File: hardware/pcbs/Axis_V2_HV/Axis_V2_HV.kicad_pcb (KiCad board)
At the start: 2 copper layers, 86.4 x 66 mm, 28 parts, among them J1 SWD, J2 UART, J3 Conn_01x02, J4 Conn_01x02, J5 Conn_01x04, J6 Conn_01x10, J7 Conn_01x08, SW1 RES, U1 Pico, U2 MAX31855EASA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

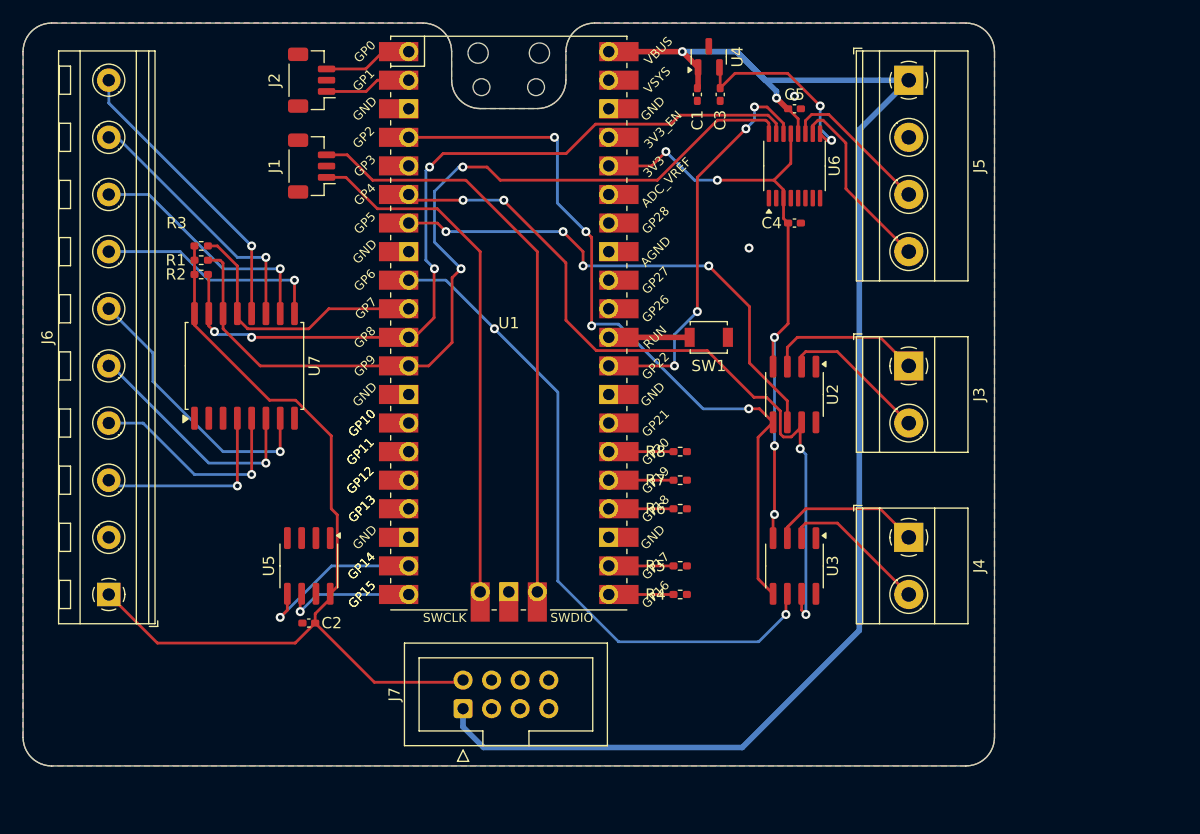
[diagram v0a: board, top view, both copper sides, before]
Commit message: Updates to V2 pcb, add HV pcb
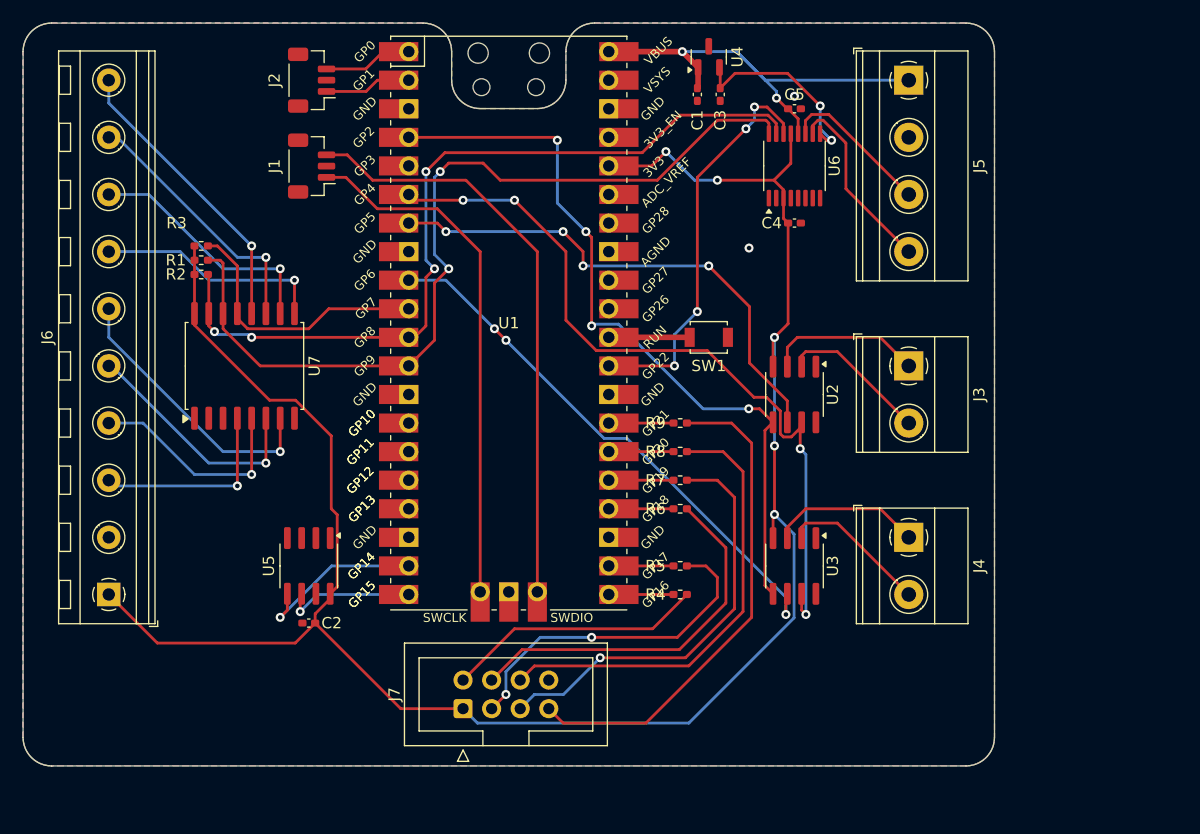
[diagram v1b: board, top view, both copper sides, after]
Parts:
- added R9: 1k, Resistor_SMD:R_0402_1005Metric_Pad0.72x0.64mm_HandSolder, F.Cu at (115.9, 55.6)
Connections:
- J7 pad 1: +5V -> +3V3
- J7 pad 2: +3V3 -> Net-(J7-Pin_2)
- R4 pad 1: Net-(J7-Pin_3) -> Net-(J7-Pin_2)
- R5 pad 1: Net-(J7-Pin_4) -> Net-(J7-Pin_3)
- R6 pad 1: Net-(J7-Pin_5) -> Net-(J7-Pin_4)
- R7 pad 1: Net-(J7-Pin_6) -> Net-(J7-Pin_5)
- R8 pad 1: Net-(J7-Pin_7) -> Net-(J7-Pin_6)
- U1 pad 27: unconnected-(U1-GPIO21-Pad27) -> /HV_IO6
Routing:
- net +5V: track 133.8 -> 41.2 mm
- net +3V3: track 133.8 -> 178.4 mm
- net Net-(J7-Pin_7): track 0.00 -> 44.4 mm
- net Net-(J7-Pin_6): track 0.00 -> 40.5 mm
- net Net-(J7-Pin_5): track 0.00 -> 37.5 mm, vias 0 -> 1
- net Net-(J7-Pin_4): track 0.00 -> 33.5 mm
- net Net-(J7-Pin_3): track 0.00 -> 30.3 mm, vias 0 -> 2
- net Net-(J7-Pin_2): track 0.00 -> 23.1 mm
- net /SPI0_CS1: track 59.6 -> 48.6 mm, vias 2 -> 3
- net /HV_IO6: track 0.00 -> 5.75 mm
- net /I2C0_SCL: track 78.9 -> 78.0 mm
- net /SPI0_RX: track 68.2 -> 68.7 mm
- net /SPI0_SCK: track 67.2 -> 66.7 mm

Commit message: Updates to the HV pcb
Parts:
- removed C1, C2, C3, C4, C5: 0.1u, Capacitor_SMD:C_0402_1005Metric_Pad0.74x0.62mm_HandSolder
- removed J1: SWD, Connector_JST:JST_SH_BM03B-SRSS-TB_1x03-1MP_P1.00mm_Vertical
- removed J2: UART, Connector_JST:JST_SH_BM03B-SRSS-TB_1x03-1MP_P1.00mm_Vertical
- removed J3, J4: Conn_01x02, TerminalBlock_Phoenix:TerminalBlock_Phoenix_MKDS-1,5-2-5.08_1x02_P5.08mm_Horizontal
- removed J5: Conn_01x04, TerminalBlock_Phoenix:TerminalBlock_Phoenix_MKDS-1,5-4-5.08_1x04_P5.08mm_Horizontal
- removed J6: Conn_01x10, TerminalBlock_RND:TerminalBlock_RND_205-00240_1x10_P5.08mm_Horizontal
- removed J7: Conn_01x08, Connector_IDC:IDC-Header_2x04_P2.54mm_Vertical
- removed R1, R2, R3, R4, R5, R6, R7, R8, R9: 1k, Resistor_SMD:R_0402_1005Metric_Pad0.72x0.64mm_HandSolder
- removed SW1: RES, Button_Switch_SMD:SW_SPST_B3U-1000P
- removed U1: Pico, MCU_RaspberryPi_and_Boards:RPi_Pico_SMD_TH
- removed U2, U3: MAX31855EASA, Package_SO:SOIC-8_3.9x4.9mm_P1.27mm
- removed U4: MAX6107, Package_TO_SOT_SMD:SOT-23
- removed U5: FM24CL16B, Package_SO:SOIC-8_3.9x4.9mm_P1.27mm
- removed U6: ADS1119IPWR, Package_SO:TSSOP-16_4.4x5mm_P0.65mm
- removed U7: TCA9534, Package_SO:SOIC-16W_7.5x10.3mm_P1.27mm
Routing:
- net +3V3: track 178.4 -> 0.00 mm, vias 5 -> 0
- net /I2C0_SCL: track 78.0 -> 0.00 mm, vias 2 -> 0
- net /I2C0_SDA: track 73.5 -> 0.00 mm, vias 4 -> 0
- net /SPI0_RX: track 68.7 -> 0.00 mm, vias 4 -> 0
- net /SPI0_SCK: track 66.7 -> 0.00 mm, vias 4 -> 0
- net /SWDIO: track 52.6 -> 0.00 mm
- net /SPI0_CS1: track 48.6 -> 0.00 mm, vias 3 -> 0
- net /SWCLK: track 46.6 -> 0.00 mm
- net /SPI0_CS0: track 45.8 -> 0.00 mm, vias 4 -> 0
- net Net-(J7-Pin_7): track 44.4 -> 0.00 mm
- net +5V: track 41.2 -> 0.00 mm, vias 2 -> 0
- net Net-(J7-Pin_6): track 40.5 -> 0.00 mm
- net Net-(J7-Pin_5): track 37.5 -> 0.00 mm, vias 1 -> 0
- net /~{I2C0_ADS_RDY}: track 35.9 -> 0.00 mm, vias 4 -> 0
- net Net-(J7-Pin_4): track 33.5 -> 0.00 mm
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- removed copper zone on B.Cu, net GND
- removed copper zone on F.Cu, net GND
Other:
- board outline removed
- board text removed: "GP10"
- board text removed: "GP11"
- board text removed: "GP12"
- board text removed: "GP13"
- board text removed: "GP14"
- board text removed: "GP15"

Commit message: Is anyone listening anymore?
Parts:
- added C1: 10u, Capacitor_SMD:C_1206_3216Metric, B.Cu at (154.6, 56.6)
- added C2: 1n, Capacitor_SMD:C_1206_3216Metric, B.Cu at (152.0, 43.6)
- added C3: 0.1u, Capacitor_THT:C_Rect_L13.0mm_W6.0mm_P10.00mm_FKS3_FKP3_MKS4, F.Cu at (142.0, 46.0)
- added C4: 0.1u, Capacitor_THT:C_Rect_L13.0mm_W6.0mm_P10.00mm_FKS3_FKP3_MKS4, F.Cu at (116.0, 46.0)
- added C7: 0.1u, Capacitor_SMD:C_0402_1005Metric, B.Cu at (78.0, 79.0)
- added D1: MB6S, Package_TO_SOT_SMD:TO-269AA, B.Cu at (152.0, 49.0)
- added D2: 1N4148W, Diode_SMD:D_SOD-123, B.Cu at (149.8, 61.8)
- added F1: Fuse (3A, slow), Fuse:Fuseholder_Cylinder-5x20mm_Schurter_0031_8201_Horizontal_Open, F.Cu at (86.0, 40.0)
- added F2: Fuse (1A, Slow), Fuse:Fuseholder_Cylinder-5x20mm_Schurter_0031_8201_Horizontal_Open, F.Cu at (124.0, 62.5)
- added F3: Fuse (1A, Slow), Fuse:Fuseholder_Cylinder-5x20mm_Schurter_0031_8201_Horizontal_Open, F.Cu at (98.0, 62.5)
- added H1: MountingHole, MountingHole:MountingHole_2.7mm_M2.5, F.Cu at (64.0, 34.0)
- added H2: MountingHole, MountingHole:MountingHole_2.7mm_M2.5, F.Cu at (64.0, 86.0)
- added H3: MountingHole, MountingHole:MountingHole_2.7mm_M2.5, F.Cu at (156.0, 34.0)
- added H4: MountingHole, MountingHole:MountingHole_2.7mm_M2.5, F.Cu at (156.0, 86.0)
- added J1: Conn_01x08, Connector_IDC:IDC-Header_2x04_P2.54mm_Vertical, F.Cu at (86.2, 84.8)
- added J2: AC, TerminalBlock_Phoenix:TerminalBlock_Phoenix_MKDS-1,5-2-5.08_1x02_P5.08mm_Horizontal, F.Cu at (77.1, 36.0)
- added J3: PUMP, TerminalBlock_Phoenix:TerminalBlock_Phoenix_MKDS-1,5-2-5.08_1x02_P5.08mm_Horizontal, F.Cu at (139.5, 36.0)
- added J4: 3WAY, TerminalBlock_Phoenix:TerminalBlock_Phoenix_MKDS-1,5-2-5.08_1x02_P5.08mm_Horizontal, F.Cu at (113.0, 36.0)
- added J5: SSR, TerminalBlock_Phoenix:TerminalBlock_Phoenix_MKDS-1,5-2-5.08_1x02_P5.08mm_Horizontal, F.Cu at (65.7, 73.5)
- added J6: PWR, TerminalBlock_Phoenix:TerminalBlock_Phoenix_MKDS-1,5-2-5.08_1x02_P5.08mm_Horizontal, F.Cu at (65.8, 61.5)
- added OC1: 4N35, Package_DIP:SMDIP-6_W7.62mm, B.Cu at (152.0, 70.0)
- added Q1: MMBT3904, Package_TO_SOT_SMD:SOT-23, B.Cu at (153.4, 61.8)
- added Q2: BC847, Package_TO_SOT_SMD:SOT-23, B.Cu at (142.8, 80.5)
- added Q3: BC847, Package_TO_SOT_SMD:SOT-23, B.Cu at (126.0, 80.1)
- added R1: 1k, Resistor_SMD:R_0402_1005Metric, B.Cu at (109.0, 85.8)
- added R10: 220, Resistor_THT:R_Axial_DIN0207_L6.3mm_D2.5mm_P10.16mm_Horizontal, F.Cu at (142.0, 62.1)
- added R11: 1k, Resistor_SMD:R_0402_1005Metric, B.Cu at (141.8, 85.8)
- added R12: 162, Resistor_SMD:R_0603_1608Metric, B.Cu at (121.2, 79.6)
- added R13: 220, Resistor_THT:R_Axial_DIN0207_L6.3mm_D2.5mm_P10.16mm_Horizontal, F.Cu at (116.0, 62.1)
- added R14: 1k, Resistor_SMD:R_0402_1005Metric, B.Cu at (125.0, 83.6)
- added R2: 1k, Resistor_SMD:R_0402_1005Metric, B.Cu at (109.0, 83.2)
- added R3: 1k, Resistor_SMD:R_0402_1005Metric, B.Cu at (109.0, 81.2)
- added R4: 1k, Resistor_SMD:R_0402_1005Metric, B.Cu at (109.0, 79.2)
- added R5: 1k, LED_SMD:LED_1206_3216Metric, B.Cu at (150.6, 57.8)
- added R6: 220k, Resistor_THT:R_Axial_DIN0207_L6.3mm_D2.5mm_P10.16mm_Horizontal, F.Cu at (146.6, 48.8)
- added R7: 22k, Resistor_SMD:R_1206_3216Metric, B.Cu at (150.6, 55.0)
- added R8: 220k, Resistor_THT:R_Axial_DIN0207_L6.3mm_D2.5mm_P10.16mm_Horizontal, F.Cu at (157.4, 48.8)
- added R9: 162, Resistor_SMD:R_0603_1608Metric, B.Cu at (137.2, 79.0)
- added RV1: MOV-10D471K, Varistor:RV_Disc_D12mm_W7.5mm_P7.5mm, F.Cu at (137.0, 53.2)
- added RV2: MOV-10D471K, Varistor:RV_Disc_D12mm_W7.5mm_P7.5mm, F.Cu at (111.0, 53.2)
- added U1: AQH3213, Package_DIP:DIP-8-N7_W7.62mm, F.Cu at (134.2, 73.8)
- added U2: PCA9536DP, Package_SO:TSSOP-8_3x3mm_P0.65mm, B.Cu at (77.0, 83.8)
- added U3: AQH3213, Package_DIP:DIP-8-N7_W7.62mm, F.Cu at (108.2, 73.8)
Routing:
- net /AC_NEG: track 0.00 -> 69.5 mm
- net /AC_P: track 0.00 -> 64.0 mm
- net /PUMP_L: track 0.00 -> 36.2 mm
- net /3WAY_L: track 0.00 -> 36.0 mm
- net /AC_POS: track 0.00 -> 30.1 mm
- net Net-(F3-Pad1): track 0.00 -> 25.1 mm
- net Net-(F2-Pad1): track 0.00 -> 25.1 mm
- net Net-(D1--): track 0.00 -> 17.4 mm, vias 0 -> 2
- net Net-(OC1-Pad1): track 0.00 -> 9.82 mm
- net Net-(D1-+): track 0.00 -> 8.84 mm
- net Net-(C2-Pad2): track 0.00 -> 7.71 mm
- net Net-(C2-Pad1): track 0.00 -> 7.71 mm
- net Net-(D2-A): track 0.00 -> 7.13 mm
- net Net-(C4-Pad1): track 0.00 -> 5.92 mm
- net Net-(C3-Pad1): track 0.00 -> 5.92 mm
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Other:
- board outline added: 100 x 60 mm

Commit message: Yuuuuuuuuuuuuuuuuuup, nobody's here
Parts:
- R5: footprint LED_SMD:LED_1206_3216Metric -> Resistor_SMD:R_1206_3216Metric
- moved H2 110.9 mm to (156.0, 24.0), turned to 180 degrees
- moved H4 110.9 mm to (64.0, 24.0), turned to 180 degrees
- moved H1 101.1 mm to (156.0, 76.0), turned to 180 degrees
- moved H3 101.1 mm to (64.0, 76.0), turned to 180 degrees
- moved R8 95.6 mm to (62.6, 61.2), turned to -90 degrees
- moved J5 94.8 mm to (153.0, 36.5), turned to 90 degrees
- moved C1 89.3 mm to (65.4, 53.4), turned to 90 degrees
- moved OC1 89.2 mm to (68.0, 40.0), turned to 90 degrees
- moved J6 88.2 mm to (153.0, 48.5), turned to 90 degrees
- moved Q1 87.9 mm to (66.6, 48.2), turned to 180 degrees
- moved C2 87.0 mm to (68.0, 66.4), turned to 180 degrees
- moved R11 85.8 mm to (77.4, 29.2), turned to -90 degrees
- moved D1 84.9 mm to (68.0, 61.0), turned to 90 degrees
- moved U2 81.7 mm to (143.0, 35.6), turned to 180 degrees
- moved R5 81.4 mm to (69.4, 52.2), turned to 0 degrees
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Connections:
- J1 pad 4: /ZC_SIG -> /~{ZC_SIG}
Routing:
- net GND: track 0.00 -> 117.6 mm, vias 0 -> 5
- net +3V3: track 0.00 -> 87.8 mm, vias 0 -> 6
- net /~{ZC_SIG}: track 0.00 -> 79.8 mm
- net /PUMP_IN: track 0.00 -> 58.7 mm
- net /AC_NEG: track 69.5 -> 103.6 mm
- net /3WAY_IN: track 0.00 -> 25.8 mm
- net /HV_SDA: track 0.00 -> 19.5 mm
- net /PWR_SW: track 0.00 -> 18.9 mm, vias 0 -> 2
- net /HV_SCL: track 0.00 -> 17.9 mm
- net Net-(Q3-C): track 0.00 -> 11.5 mm
- net Net-(Q2-C): track 0.00 -> 11.5 mm
- net /SSR: track 0.00 -> 8.38 mm
- net Net-(R9-Pad1): track 0.00 -> 2.43 mm
- net Net-(R12-Pad1): track 0.00 -> 2.43 mm
- net Net-(Q3-B): track 0.00 -> 2.01 mm
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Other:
- outline, holes or cut-outs redrawn
- board text added: "!!! DANGER, HIGH VOLTAGE !!!"
- board text added: "!!! HIGH VOLTAGE !!!"
- board text added: "3WAY"
- board text added: "L"
- board text added: "N"
- board text added: "PUMP"

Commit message: Ok I'm about to order the HV pcb and parts somebody stop me
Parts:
- moved J4 0.20 mm to (107.0, 73.2)
- moved J2 0.20 mm to (142.9, 73.2)
- moved J3 0.20 mm to (80.5, 73.2)
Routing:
- net /AC_NEG: track 103.6 -> 106.4 mm
- net GND: track 117.6 -> 120.3 mm
- net /~{ZC_SIG}: track 79.8 -> 78.7 mm
- net /PWR_SW: track 18.9 -> 19.4 mm
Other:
- board text added: "+3v3"
- board text added: "Axis HV PCB github.com/Meigs2/Axis"
- board text added: "GND"
- board text added: "SSR"
- board text added: "SW"
